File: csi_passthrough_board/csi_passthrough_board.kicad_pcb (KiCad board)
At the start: 4 copper layers, 148.5 x 148.3 mm, 23 parts, among them J1 CSI-22-F32Q-1A7H1-11022, J10 Screw_Terminal_01x05, J101 CSI-22-F32Q-1A7H1-11022, J102 CSI-22-F32Q-1A7H1-11022, J103 CSI-22-F32Q-1A7H1-11022, J104 CSI-22-F32Q-1A7H1-11022, J105 CSI-22-F32Q-1A7H1-11022, J106 CSI-22-F32Q-1A7H1-11022, J107 CSI-22-F32Q-1A7H1-11022, J108 CSI-22-F32Q-1A7H1-11022, J2 CSI-22-F32Q-1A7H1-11022, J3 CSI-22-F32Q-1A7H1-11022, J4 CSI-22-F32Q-1A7H1-11022, J5 CSI-22-F32Q-1A7H1-11022, J6 CSI-22-F32Q-1A7H1-11022, J7 CSI-22-F32Q-1A7H1-11022, J8 CSI-22-F32Q-1A7H1-11022

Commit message: Add files via upload
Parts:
- moved J3 4.00 mm to (171.3, 140.5)
- moved J2 2.50 mm to (221.3, 97.0)
- moved J4 2.00 mm to (121.3, 96.5)
- moved U1 0.06 mm to (142.8, 102.6)
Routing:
- net GND: track 180.9 -> 185.3 mm, vias 159 -> 157
- net /CAM3-SDA: track 41.9 -> 37.5 mm
- net /CAM3-POWER-EN: track 45.3 -> 41.3 mm
- net /CAM2-POWER-EN: track 45.6 -> 42.2 mm
- net /CAM3-LED-EN: track 43.2 -> 40.1 mm
- net /CAM2-LED-EN: track 44.7 -> 41.8 mm
- net /CAM3-SCL: track 41.1 -> 38.3 mm
- net /CAM2-SDA: track 43.1 -> 40.6 mm
- net /CAM2-SCL: track 43.6 -> 41.1 mm
- net /CAM2-VCC: track 42.7 -> 40.5 mm
- net /CAM4_D1_P: track 88.3 -> 90.3 mm
- net /CAM4_D1_N: track 88.3 -> 90.3 mm
- net /CAM4_D0_P: track 88.3 -> 90.3 mm
- net /CAM4_D0_N: track 88.3 -> 90.3 mm
- net /CAM4_CK_P: track 88.3 -> 90.3 mm
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
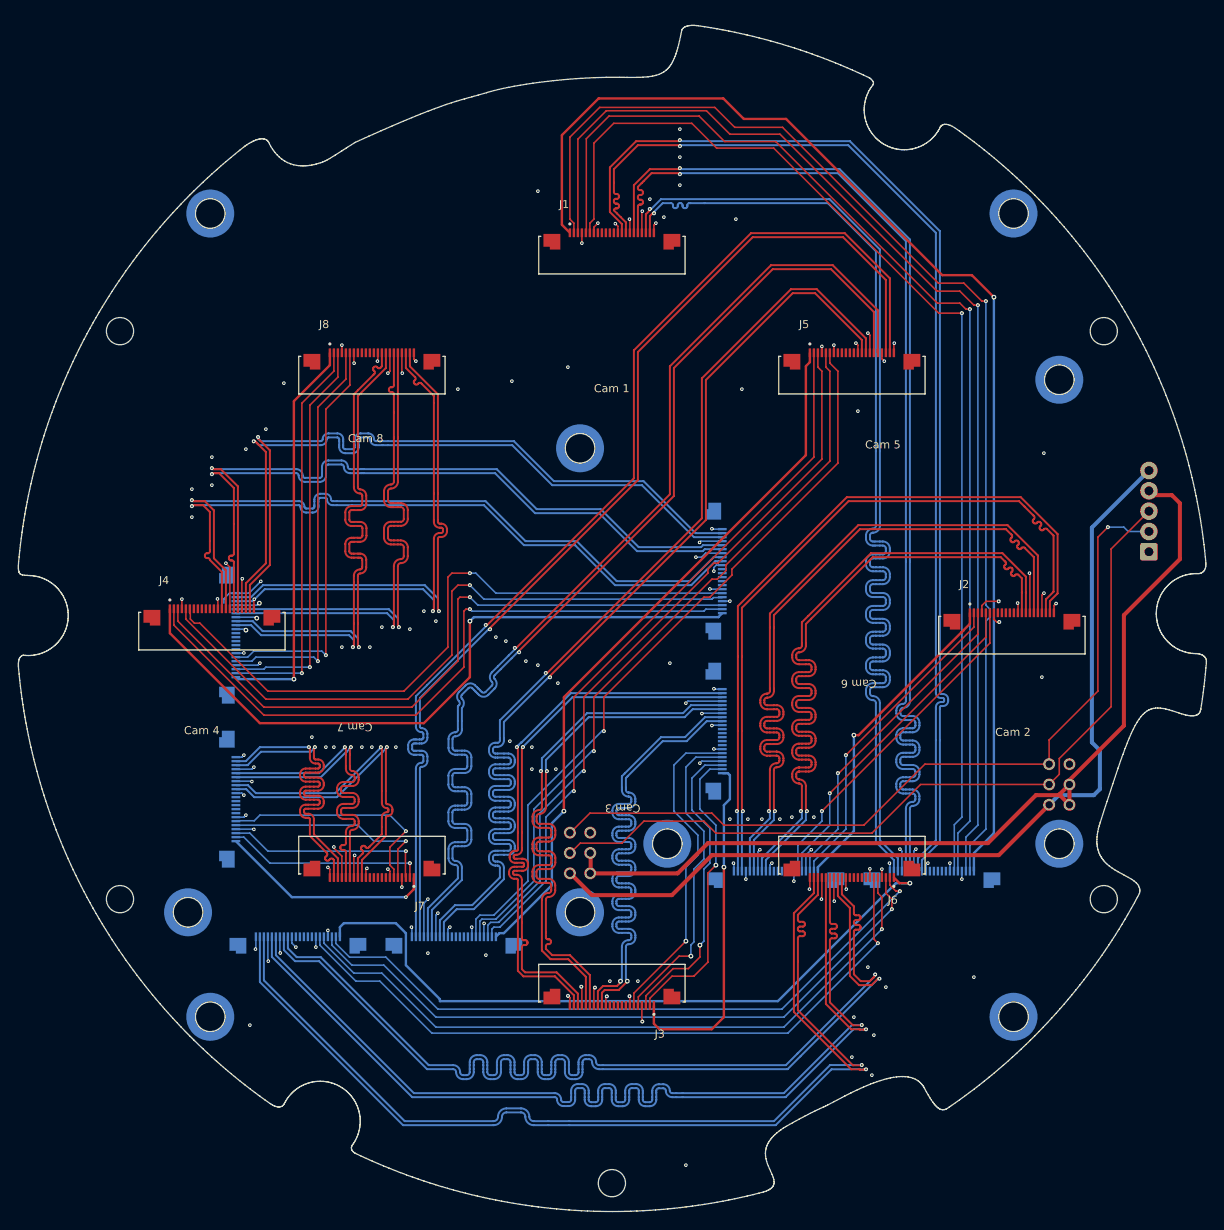
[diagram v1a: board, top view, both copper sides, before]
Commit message: changed screw terminal location and mounting hole locatoin
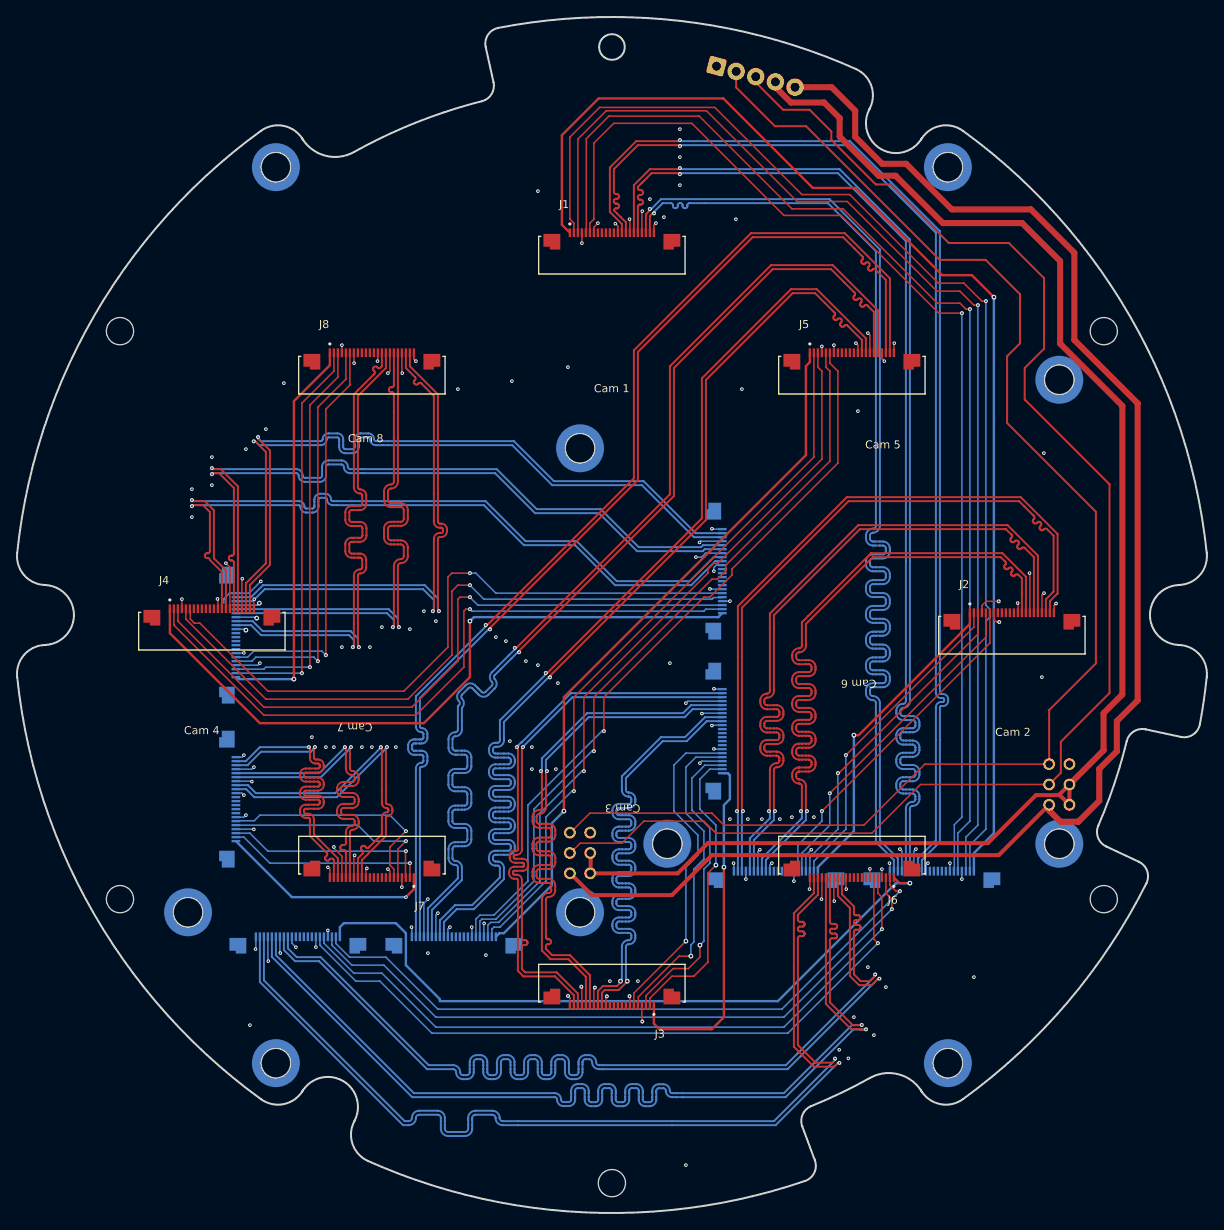
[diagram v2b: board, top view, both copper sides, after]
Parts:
- moved J10 81.3 mm to (184.4, 25.9), turned to -15 degrees
- moved MP1 10.0 mm to (129.3, 38.5)
- moved MP3 10.0 mm to (213.3, 38.5)
- moved MP2 10.0 mm to (129.3, 150.5)
- moved MP4 10.0 mm to (213.3, 150.5)
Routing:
- net /SDA: track 104.0 -> 184.0 mm
- net +3V3: track 116.0 -> 193.5 mm
- net /SCL: track 102.7 -> 179.3 mm, vias 1 -> 0
- net +5V: track 116.7 -> 189.3 mm
- net /CAM5_CK_P: track 136.3 -> 137.9 mm
- net /CAM5_D0_P: track 136.7 -> 138.2 mm
- net /CAM5_D1_P: track 136.3 -> 137.9 mm
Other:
- board size 148.5 x 148.3 mm -> 148.7 x 149.5 mm
- board text added: "CSI Pass-Through Board V1.3"
- board text added: "GND SCL SDA 5V 3V3"
- board text removed: "3V3 5V SDA SCL GND"
- board text removed: "CSI Pass-Through Board V1.2"

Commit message: before updating headers
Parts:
- moved MP1 10.0 mm to (121.1, 44.3)
- moved MP3 10.0 mm to (221.5, 44.3)
- moved MP2 10.0 mm to (121.1, 144.7)
- moved MP4 10.0 mm to (221.5, 144.7)
- moved J6 1.00 mm to (201.3, 123.5)
- moved J7 1.00 mm to (141.3, 123.5)
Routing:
- net /SCL: track 179.3 -> 228.4 mm
- net /SDA: track 184.0 -> 228.7 mm
- net +5V: track 189.3 -> 194.9 mm, vias 0 -> 2
- net /CAM6-VCC: track 87.6 -> 92.2 mm
- net GND: track 185.3 -> 189.8 mm
- net /CAM6-SDA: track 83.4 -> 86.4 mm
- net /CAM7_D0_N: track 40.2 -> 37.2 mm
- net /CAM7_D1_N: track 40.2 -> 37.3 mm
- net /CAM7_CK_N: track 40.4 -> 37.5 mm
- net /CAM6-SCL: track 84.6 -> 86.8 mm
- net /CAM7-VCC: track 27.0 -> 29.0 mm
- net /CAM7_D0_P: track 40.2 -> 38.2 mm
- net /CAM7_D1_P: track 40.2 -> 38.3 mm
- net /CAM7_CK_P: track 40.4 -> 38.5 mm
- net /CAM7-POWER-EN: track 29.2 -> 27.8 mm
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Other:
- board text added: "CSI Pass-Through Board V1.4"
- board text removed: "CSI Pass-Through Board V1.3"

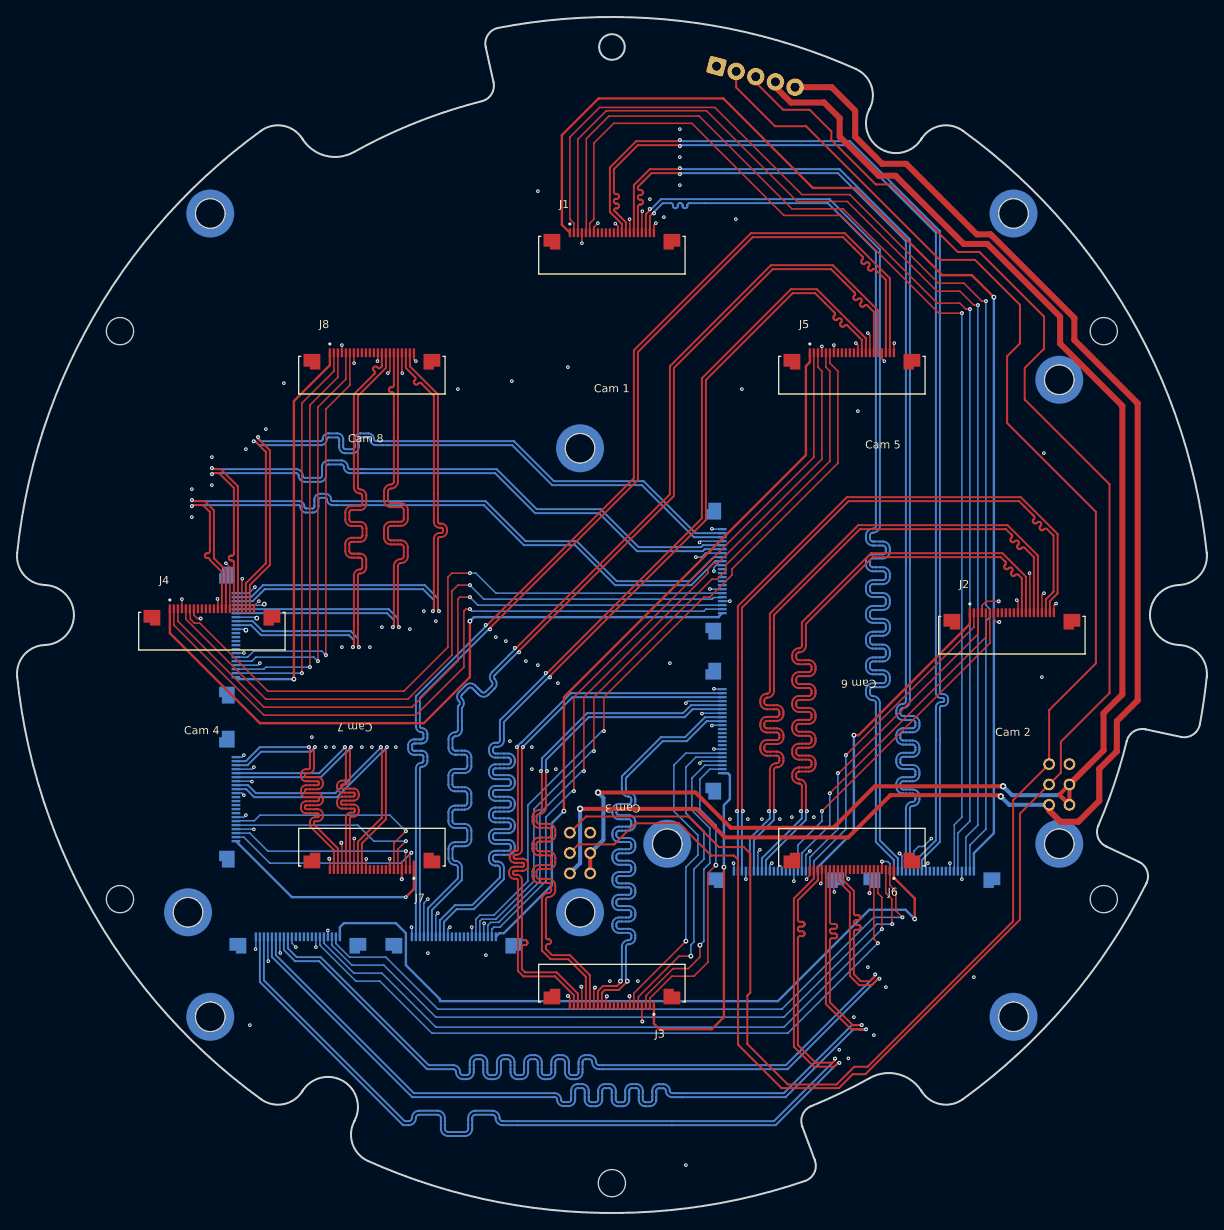
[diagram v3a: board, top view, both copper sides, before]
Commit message: V1.4, added bottom entry pins
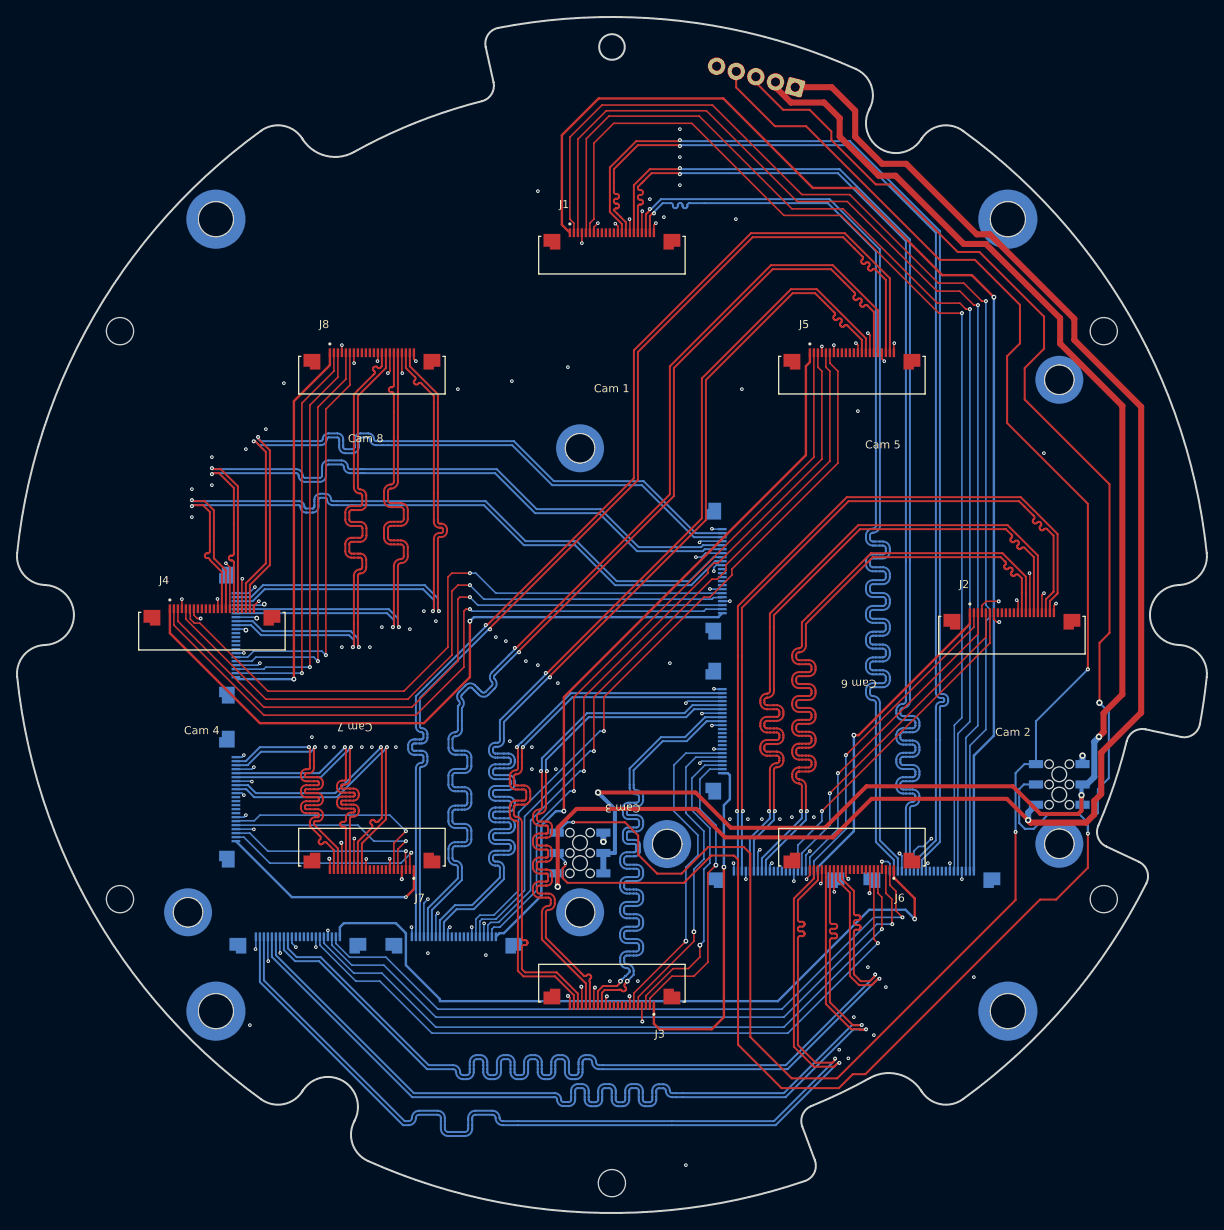
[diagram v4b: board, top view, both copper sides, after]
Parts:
- added J11: M20-7810345, M20_7810345:HARWIN_M20-7810345, B.Cu at (227.2, 115.6)
- added J9: M20-7810345, M20_7810345:HARWIN_M20-7810345, B.Cu at (167.3, 124.2)
- added MP10: M2.5 x 4mm, 9774040151R:WA-SMSI_9774040151, B.Cu at (227.2, 65.1)
- added MP5: M2.5 x 4mm, 9774040151R:WA-SMSI_9774040151, B.Cu at (118.3, 131.6)
- added MP6: M2.5 x 4mm, 9774040151R:WA-SMSI_9774040151, B.Cu at (167.3, 131.6)
- added MP7: M2.5 x 4mm, 9774040151R:WA-SMSI_9774040151, B.Cu at (167.3, 73.6)
- added MP8: M2.5 x 4mm, 9774040151R:WA-SMSI_9774040151, B.Cu at (178.2, 123.1)
- added MP9: M2.5 x 4mm, 9774040151R:WA-SMSI_9774040151, B.Cu at (227.2, 123.1)
- J1, J101, J102, J103, J104, J105, J106, J107, J108, J2, J3, J4, J5, J6, J7, J8: footprint lachs_lib:AMPHENOL_F32Q-1A7H1-11022 -> F32Q_1A7H1_11022:AMPHENOL_F32Q-1A7H1-11022
- MP1, MP2, MP3, MP4: value M2.5 x 3.5mm -> M2.5 x 12mm; footprint WA-SMSI_9774XXX151:WA-SMSI_9774035151 -> 9774120360R:WA-SMSI_9774120360
- U1, U2: value ~ -> CSI Mux Hat; footprint lachs_lib:CSI_Mux_Hat -> CSI_Mux_hat:CSI_Mux_Hat
- moved J10 10.2 mm to (194.2, 28.5), turned to 165 degrees
- moved MP2 1.00 mm to (121.8, 144.0)
- moved MP1 1.00 mm to (121.8, 45.0)
- moved MP4 1.00 mm to (220.8, 144.0)
- moved MP3 1.00 mm to (220.8, 45.0)
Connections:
- J10 pad 1: GND -> +3V3
- J10 pad 2: /SCL -> +5V
- J10 pad 4: +5V -> /SCL
- J10 pad 5: +3V3 -> GND
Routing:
- net /SDA: track 228.7 -> 251.9 mm, vias 0 -> 3
- net +3V3: track 194.5 -> 201.3 mm
- net /SCL: track 228.4 -> 230.5 mm, vias 0 -> 3
- net GND: track 189.8 -> 191.0 mm, vias 157 -> 158
- net +5V: track 194.9 -> 195.9 mm, vias 2 -> 3
- net /CAM7-VCC: track 29.0 -> 28.0 mm
- net /CAM7_D0_N: track 37.2 -> 38.2 mm
- net /CAM7_D1_N: track 37.3 -> 38.3 mm
- net /CAM7_CK_N: track 37.5 -> 38.5 mm
- net /CAM3-LED-EN: track 40.1 -> 39.2 mm
- net /CAM5-VCC: track 89.6 -> 90.2 mm
- net /CAM3_CK_P: track 69.2 -> 69.7 mm
